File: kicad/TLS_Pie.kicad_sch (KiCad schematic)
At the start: 23 parts, among them M1 stepper + 50:1, U1 DS3231 breakout, U10 fan 5 V, U11 INA226 -- NOT FITTED, U12 BCD5A -> 16.8 V / 1.5 A (17.0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, U3 LM2596S-ADJ -> 5.1 V, U4 Big Easy Driver, U7 VLP-16 interface box, U8 Velodyne VLP-16

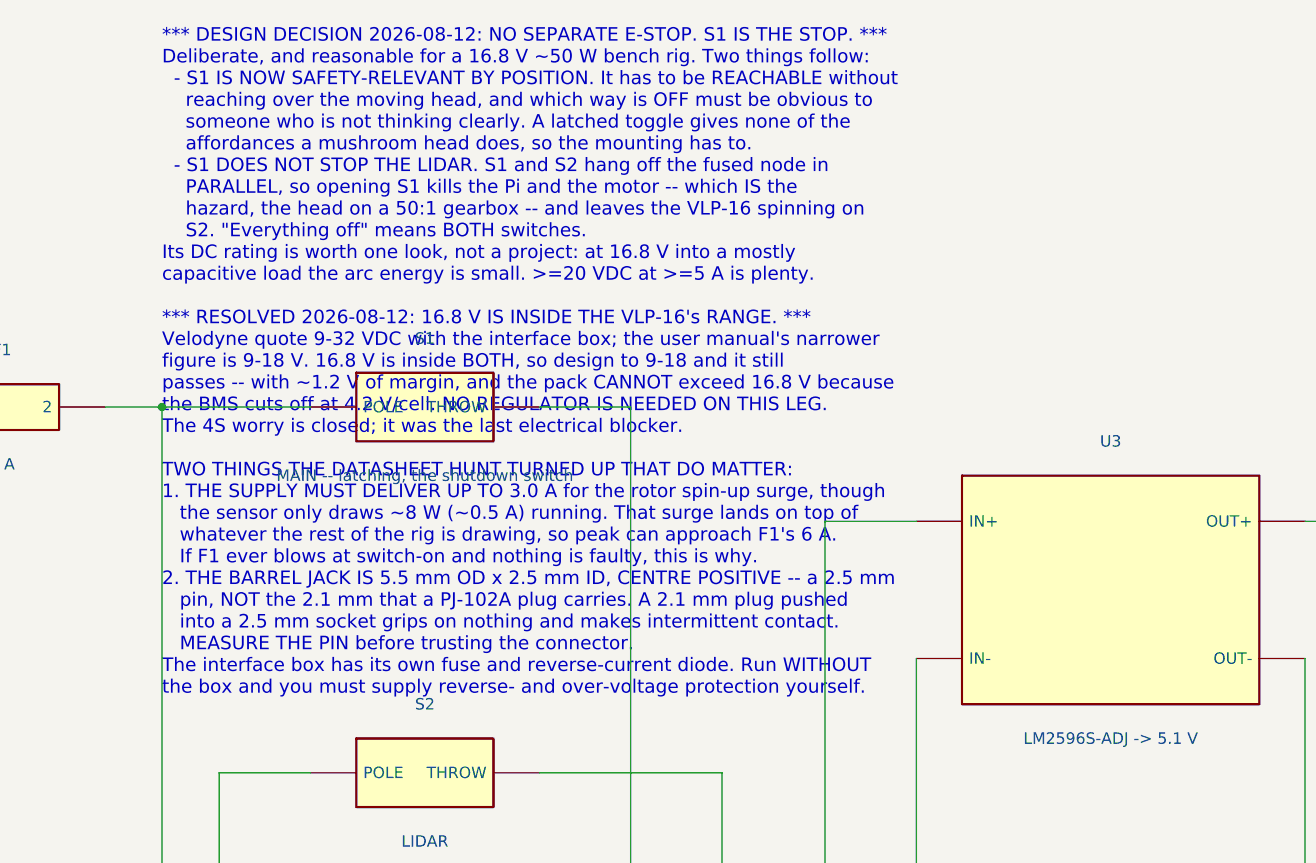
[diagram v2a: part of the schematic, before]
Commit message: Drop the E-stop from the design entirely: S1 is the main power switch
Operator's instruction, 2026-08-13: "forget about the e-stop completely,
i have a main power switch." It had already been decided against on
08-12, but the analysis behind that decision stayed written down in nine
places across the record, the wiring procedure, the schematic and the
source -- so every session read it as an open question and raised it
again. This session raised it again. Removing the text is the fix; the
agreement was never the problem.

Cleared from:
  PROJECT_CONTEXT.md      seven passages, plus the two derived to-do
                          items (S1's mounting position, S1's DC rating)
  WIRING_REV3_BMS.html    the "No separate E-stop" note box
  kicad/                  the schematic sheet note, regenerated
  tls_scan.py             "Fit a LATCHING E-STOP" in BEFORE FIRST RUN,
                          and the pointer to the DC rating caveat
  tls_web.py              the module SAFETY block -- and the page footer,
                          which was USER-VISIBLE: the panel told the
                          operator to fit an E-stop on every visit
  tls_stepper.py          "hardware emergency stop" wording

What is kept, because it is plumbing rather than safety argument: S1 and
S2 hang off the fused node in parallel, so "everything off" means both
switches. And the honest limit of the software stop is kept too, minus
the recommendation: if the controller dies while pigpio's DMA engine is
clocking steps, cutting power is what stops the motor.

Schematic regenerated, 2186 validator checks pass. 67 + 23 + 80 tests
pass. Deployed and the panel serves 200.

Co-Authored-By: Claude Opus 5 <noreply@anthropic.com>
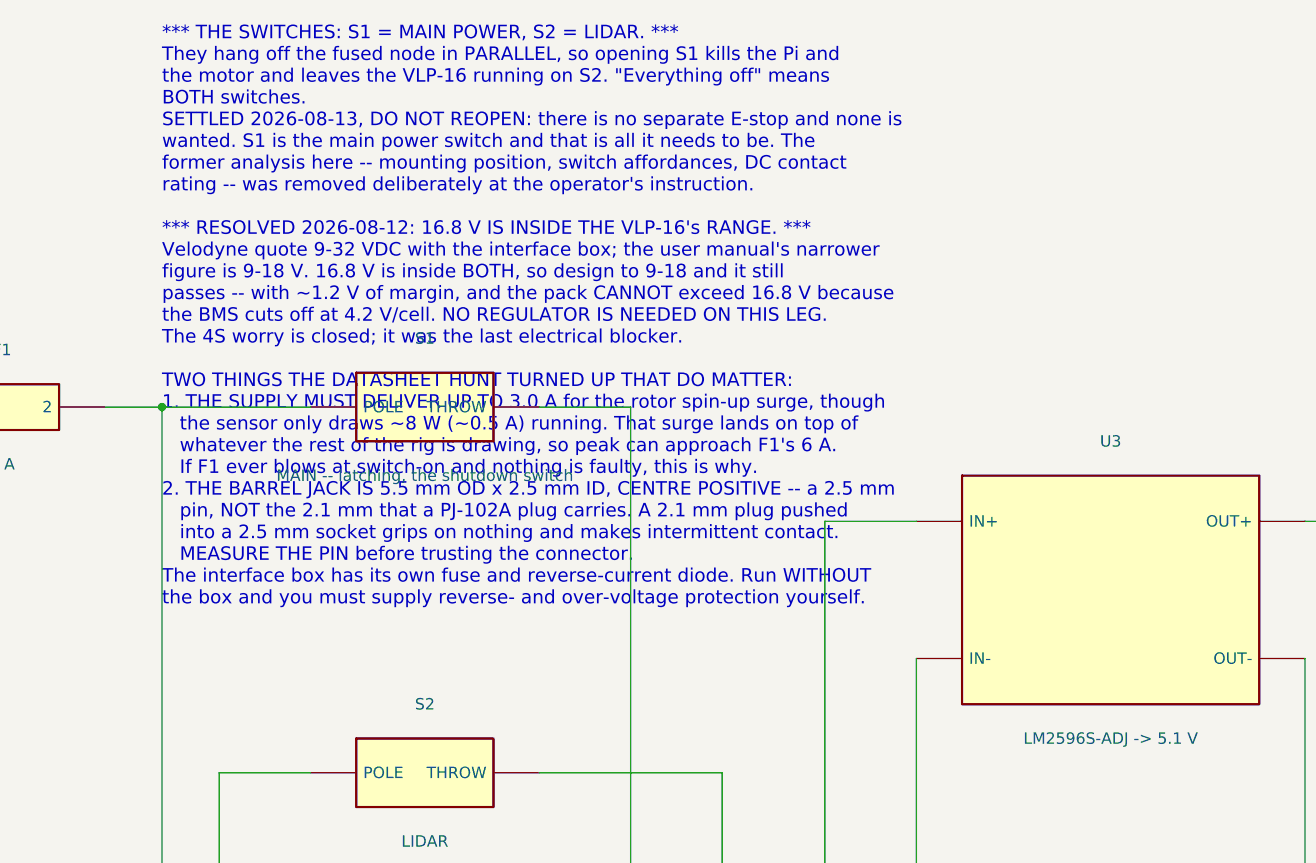
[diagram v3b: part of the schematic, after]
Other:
- note added: "*** THE SWITCHES: S1 = MAIN POWER, S2 = LIDAR. *** They hang off the fused node in PARALLEL, so opening S1 kills the Pi and the motor and leaves the VLP-16 running on S2. "Everything off" means BOTH switches. SETTLED 2026-08-13, DO NOT REOPEN: there is no separate E-stop and none is wanted. S1 is the main power switch and that is all it needs to be. The former analysis here -- mounting position, 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"
- note removed: "*** DESIGN DECISION 2026-08-12: NO SEPARATE E-STOP. S1 IS THE STOP. *** Deliberate, and reasonable for a 16.8 V ~50 W bench rig. Two things follow: - S1 IS NOW SAFETY-RELEVANT BY POSITION. It has to be REACHABLE without reaching over the moving head, and which way is OFF must be obvious to someone who is not thinking clearly. A latched toggle gives none of the affordances a mushroom head does, so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"
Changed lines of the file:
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@@
   (wire (pts (xy 481.33 99.06) (xy 524.51 99.06)) (stroke (width 0) (type default)))
   (wire (pts (xy 524.51 99.06) (xy 524.51 86.36)) (stroke (width 0) (type default)))
-  (text "*** DESIGN DECISION 2026-08-12: NO SEPARATE E-STOP. S1 IS THE STOP. ***\nDeliberate, and reasonable for a 16.8 V ~50 W bench rig. Two things follow:\n  - S1 IS NOW SAFETY-RELEVANT BY POSITION. It has to be REACHABLE without\n    reaching over the moving head, and which way is OFF must be obvious to\n    someone who is not thinking clearly. A latched toggle gives none of the\n    affordances a mushroom head does, so the mounting has to.\n  - S1 DOES NOT STOP THE LIDAR. S1 and S2 hang off the fused node in\n    PARALLEL, so opening S1 kills the Pi and the motor -- which IS the\n    hazard, the head on a 50:1 gearbox -- and leaves the VLP-16 spinning on\n    S2. \"Everything off\" means BOTH switches.\nIts DC rating is worth one look, not a project: at 16.8 V into a mostly\ncapacitive load the arc energy is small. >=20 VDC at >=5 A is plenty.\n\n*** RESOLVED 2026-08-12: 16.8 V IS INSIDE THE VLP-16's RANGE. ***\nVelodyne quote 9-32 VDC with the interface box; the user manual's narrower\nfigure is 9-18 V. 16.8 V is inside BOTH, so design to 9-18 and it still\npasses -- with ~1.2 V of margin, and the pack CANNOT exceed 16.8 V because\nthe BMS cuts off at 4.2 V/cell. NO REGULATOR IS NEEDED ON THIS LEG.\nThe 4S worry is closed; it was the last electrical blocker.\n\nTWO THINGS THE DATASHEET HUNT TURNED UP THAT DO MATTER:\n1. THE SUPPLY MUST DELIVER UP TO 3.0 A for the rotor spin-up surge, though\n   the sensor only draws ~8 W (~0.5 A) running. That surge lands on top of\n   whatever the rest of the rig is drawing, so peak can approach F1's 6 A.\n   If F1 ever blows at switch-on and nothing is faulty, this is why.\n2. THE BARREL JACK IS 5.5 mm OD x 2.5 mm ID, CENTRE POSITIVE -- a 2.5 mm\n   pin, NOT the 2.1 mm that a PJ-102A plug carries. A 2.1 mm plug pushed\n   into a 2.5 mm socket grips on nothing and makes intermittent contact.\n   MEASURE THE PIN before trusting the connector.\nThe interface box has its own fuse and reverse-current diode. Run WITHOUT\nthe box and you must supply reverse- and over-voltage protection yourself." (exclude_from_sim yes) (at 196.85 53.49 0) (effects (font (size 1.5 1.5)) (justify left)))
+  (text "*** THE SWITCHES: S1 = MAIN POWER, S2 = LIDAR. ***\nThey hang off the fused node in PARALLEL, so opening S1 kills the Pi and\nthe motor and leaves the VLP-16 running on S2. \"Everything off\" means\nBOTH switches.\nSETTLED 2026-08-13, DO NOT REOPEN: there is no separate E-stop and none is\nwanted. S1 is the main power switch and that is all it needs to be. The\nformer analysis here -- mounting position, switch affordances, DC contact\nrating -- was removed deliberately at the operator's instruction.\n\n*** RESOLVED 2026-08-12: 16.8 V IS INSIDE THE VLP-16's RANGE. ***\nVelodyne quote 9-32 VDC with the interface box; the user manual's narrower\nfigure is 9-18 V. 16.8 V is inside BOTH, so design to 9-18 and it still\npasses -- with ~1.2 V of margin, and the pack CANNOT exceed 16.8 V because\nthe BMS cuts off at 4.2 V/cell. NO REGULATOR IS NEEDED ON THIS LEG.\nThe 4S worry is closed; it was the last electrical blocker.\n\nTWO THINGS THE DATASHEET HUNT TURNED UP THAT DO MATTER:\n1. THE SUPPLY MUST DELIVER UP TO 3.0 A for the rotor spin-up surge, though\n   the sensor only draws ~8 W (~0.5 A) running. That surge lands on top of\n   whatever the rest of the rig is drawing, so peak can approach F1's 6 A.\n   If F1 ever blows at switch-on and nothing is faulty, this is why.\n2. THE BARREL JACK IS 5.5 mm OD x 2.5 mm ID, CENTRE POSITIVE -- a 2.5 mm\n   pin, NOT the 2.1 mm that a PJ-102A plug carries. A 2.1 mm plug pushed\n   into a 2.5 mm socket grips on nothing and makes intermittent contact.\n   MEASURE THE PIN before trusting the connector.\nThe interface box has its own fuse and reverse-current diode. Run WITHOUT\nthe box and you must supply reverse- and over-voltage protection yourself." (exclude_from_sim yes) (at 196.85 48.39 0) (effects (font (size 1.5 1.5)) (justify left)))
   (text "CONNECT THE TAPS IN THIS ORDER:  0V  4.2V  8.4V  12.6V  16.8V\nThe board names its pads by voltage, and those are FULL-CHARGE values --\nNOT what a flat pack measures. Against 0V at the measured 12.24 V total you\nshould read roughly:   0 / 3.06 / 6.12 / 9.18 / 12.24 V.\nWHAT MATTERS IS THE ORDER, evenly spaced and ascending. Meter every tap on\nthe free connector BEFORE plugging it in.\nThe protection ICs are powered from the taps. Out of order, one stage sees\nmost of the pack across single-cell inputs and dies silently -- leaving a\nboard that looks fine and protects nothing. Solder all five to the pack\nFIRST, meter the free connector, and only then plug it in.\n\n4.2V/8.4V/12.6V carry milliamps -- 22-24 AWG.  16.8V (B+) and 0V (B-) carry\nthe FULL pack current -- run those two THICK. Check the 16.8V lead: it is\nthe one that looks like a balance wire and is not.\n\n*** PAD ADJACENCY ON THE REAL BOARD -- ONE SLIP IS A FIRE ***\nRight edge, top to bottom:  16.8V | (+) | (-) | 4.2V.\n  (+) beside 16.8V   -- a bridge here is HARMLESS. They are the same copper:\n                        the ten FETs are all in the NEGATIVE leg, so the\n                        positive is never switched. MEASURED 0 ohms on the\n                        board 2026-08-11 -- this is verified, not inferred.\n  (-) beside 4.2V    -- a bridge here is the WORST SHORT ON THE BOARD. (-) is\n                        pack negative through the FETs and 4.2V is the top of\n                        group 1, so a stray strand puts a DEAD SHORT ACROSS\n                        THREE PARALLEL CELLS. No fuse is in that path and\n                        nothing protects it. Sleeve it, inspect it, and work\n                        that corner one lead at a time.\nLeave the CD and FD test pads alone." (exclude_from_sim yes) (at 34.29 160.155 0) (effects (font (size 1.5 1.5)) (justify left)))
   (text "PANEL METER PM1 -- and it changes the ground topology, so read this.\n\nITS THICK PAIR IS THE SHUNT, AND THE SHUNT IS IN THE NEGATIVE LEG. So it\ngoes in the RETURN, between the rig's ground and P- -- NOT in the +VBATT\nrail where U11 goes. GND and P- are now separate nodes joined ONLY through\nPM1. They cross twice on this sheet with no junction dot and are NOT\nconnected there. Bridge them anywhere and you short out the shunt: the\nmeter reads 0.00 A for ever and nothing warns you.\n\n*** VERIFY THE SHUNT LEG BEFORE SOLDERING ***\nMeter resistance thin-black to thick-black. NEAR ZERO = negative-leg shunt\nand this drawing is right. If instead thin-RED reads near zero to a thick\nlead, the shunt is in the POSITIVE leg -- then it belongs where U11 is, in\nthe +VBATT rail, and this corner of the sheet must be redrawn.\nThe two thick leads should read a fraction of an ohm to each other: that\nIS the shunt.\n\nTHIN BLACK GOES TO THE SAME SIDE AS THICK BLACK (P-). On most of these the\ntwo blacks are common inside the meter, so putting the thin one on the rig\nside of the shunt bridges it -- the same silent zero-amps failure.\n\nSUPPLY FROM +VSW1, NOT +VBATT. These meters draw ~20 mA continuously. On\n+VBATT that is ~0.5 Ah/day and would flatten this ~9 Ah pack in about three\nweeks of standing -- which is how it got flat the first time. On +VSW1 it\ndies with S1. VSENSE still reads TRUE PACK VOLTS because it taps +VBATT\nupstream of the switch, and it draws only microamps through its divider.\n\nReads 0.00 A while charging with S1 and S2 open. Correct: the charge return\nis on the pack side of the shunt, so charge current never crosses it.\nIts two thick leads carry the WHOLE rig's return -- mount PM1 at the BMS and\nkeep them short and heavy. The 6 A fuse is what keeps this inside its 10 A." (exclude_from_sim yes) (at 196.85 241.43 0) (effects (font (size 1.3 1.3)) (justify left)))
